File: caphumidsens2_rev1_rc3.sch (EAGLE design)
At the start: 12 parts, among them IC1 ATtiny25/45/85/13A

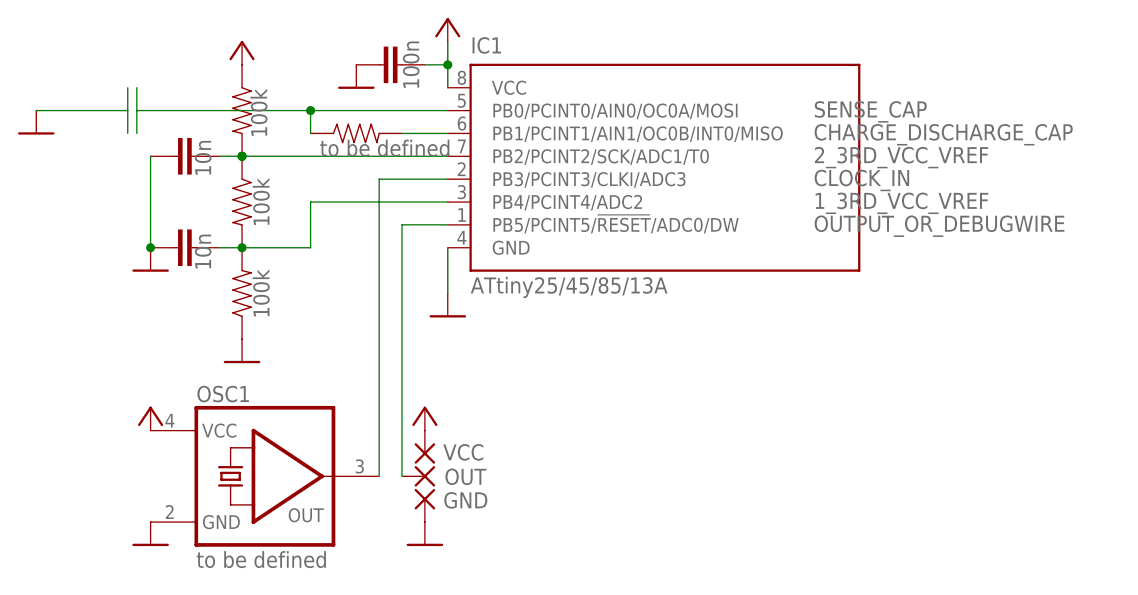
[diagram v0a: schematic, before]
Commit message: added 2nd output-pad, if osc1 isn't needed
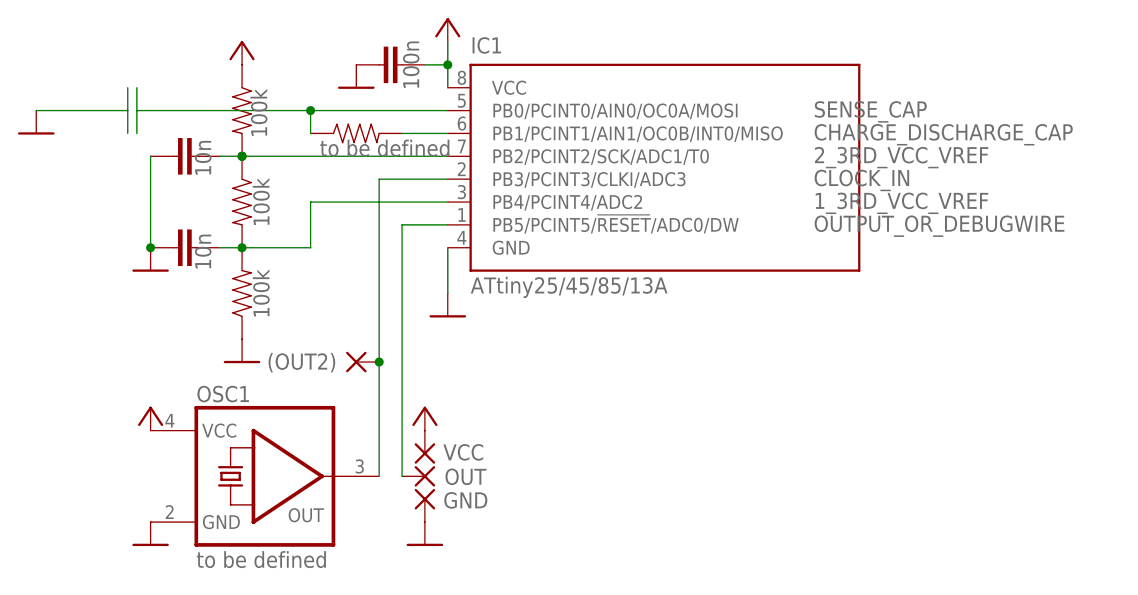
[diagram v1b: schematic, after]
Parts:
- added (OUT2): WIREPADSMD2,54-5,08, wirepad:SMD2
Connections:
- net CLOCK_IN: now also (OUT2).P
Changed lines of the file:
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@@
 <part name="GND4" library="supply1" deviceset="GND" device=""/>
 <part name="GND7" library="supply1" deviceset="GND" device=""/>
+<part name="(OUT2)" library="wirepad" deviceset="SMD2" device="" value="WIREPADSMD2,54-5,08"/>
 </parts>
 <sheets>
@@
 <instance part="GND4" gate="1" x="7.62" y="43.18" smashed="yes"/>
 <instance part="GND7" gate="1" x="20.32" y="27.94" smashed="yes"/>
+<instance part="(OUT2)" gate="1" x="43.18" y="17.78" smashed="yes">
+<attribute name="NAME" x="41.021" y="18.7198" size="1.778" layer="95" rot="R180"/>
+</instance>
 </instances>
 <busses>
@@
 <pinref part="OSC1" gate="G$1" pin="OUT"/>
 <pinref part="IC1" gate="G$1" pin="PB3/PCINT3/CLKI/ADC3"/>
-<wire x1="45.72" y1="5.08" x2="45.72" y2="38.1" width="0.1524" layer="91"/>
+<wire x1="45.72" y1="5.08" x2="45.72" y2="17.78" width="0.1524" layer="91"/>
+<wire x1="45.72" y1="17.78" x2="45.72" y2="38.1" width="0.1524" layer="91"/>
 <wire x1="45.72" y1="38.1" x2="53.34" y2="38.1" width="0.1524" layer="91"/>
 <label x="93.98" y="37.338" size="1.778" layer="95"/>
+<pinref part="(OUT2)" gate="1" pin="P"/>
+<junction x="45.72" y="17.78"/>
 </segment>
 </net>
